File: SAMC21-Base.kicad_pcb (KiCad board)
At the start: 4 copper layers, 25.4 x 42.5 mm, 52 parts, among them J1 Conn_01x04, J2 Conn_01x10, J3 Conn_01x10, J5 Conn_ARM_JTAG_SWD_10, U1 ATSAMC21E18A-AUT, U2 TJA1043T, U3 TPS560430Y, U4 MCP1703A, Y1 8MHz

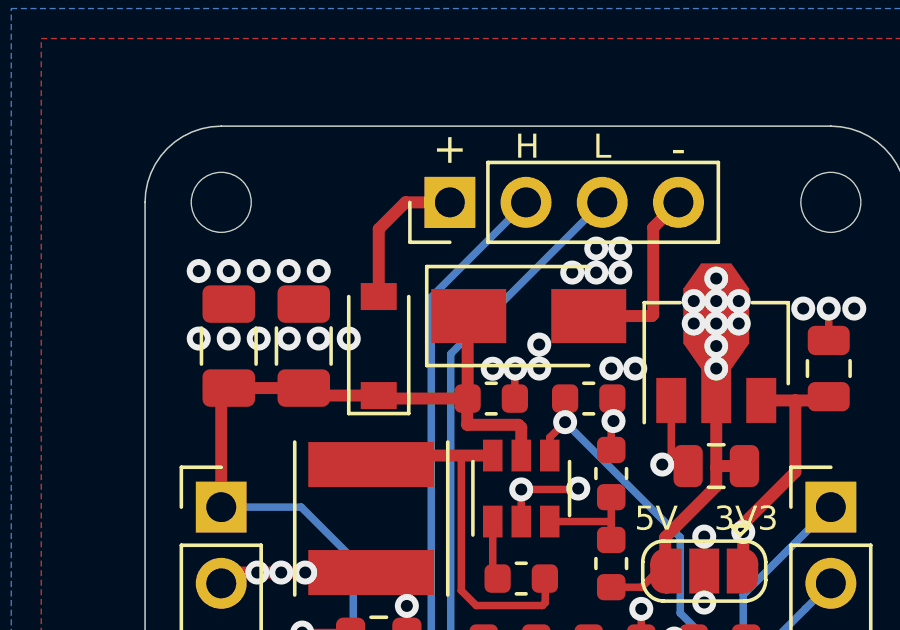
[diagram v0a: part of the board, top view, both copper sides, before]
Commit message: place ESD protection before polarity protection
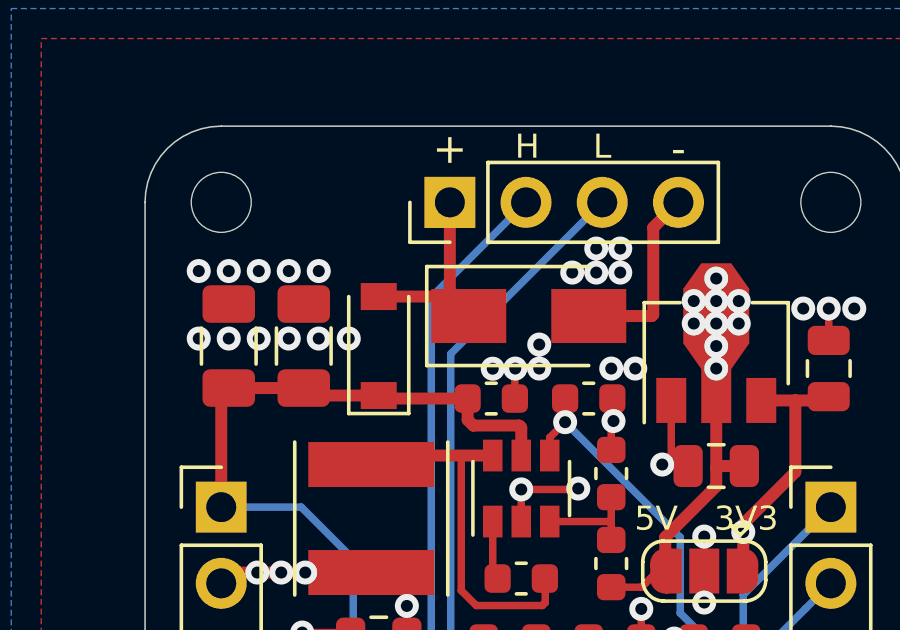
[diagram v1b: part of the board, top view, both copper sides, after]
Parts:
- L2: value L_Small -> MPZ1608S221A
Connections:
- D3 pad 1: +36V -> VBUS
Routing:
- net +36V: track 43.6 -> 40.7 mm
- net VBUS: track 4.99 -> 5.54 mm
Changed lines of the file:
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@@
     (thickness 1.6)
     (drawings 21)
-    (tracks 511)
+    (tracks 509)
     (zones 0)
     (modules 52)
@@
   )
   (setup
-    (last_trace_width 0.25)
+    (last_trace_width 0.4)
     (user_trace_width 0.25)
     (user_trace_width 0.4)
@@
       (net 43 GND))
     (pad 1 smd rect (at -2 0) (size 2.5 1.8) (layers F.Cu F.Paste F.Mask)
-      (net 2 +36V))
+      (net 12 VBUS))
     (model ${KISYS3DMOD}/Diode_SMD.3dshapes/D_SMA.wrl
       (at (xyz 0 0 0))
@@
       (effects (font (size 1 1) (thickness 0.15)))
     )
-    (fp_text value L_Small (at 0 1.43) (layer F.Fab)
+    (fp_text value MPZ1608S221A (at 0 1.43) (layer F.Fab)
       (effects (font (size 1 1) (thickness 0.15)))
     )
@@
   (segment (start 114.87 70.15) (end 114.8 70.08) (width 0.25) (layer F.Cu) (net 2))
   (segment (start 114.87 71.655) (end 114.87 70.15) (width 0.25) (layer F.Cu) (net 2))
-  (segment (start 111.6 60.85) (end 111.6 61.78) (width 0.4) (layer F.Cu) (net 2))
-  (segment (start 111.50501 60.75501) (end 111.6 60.85) (width 0.4) (layer F.Cu) (net 2))
-  (segment (start 109.8 60.75501) (end 111.50501 60.75501) (width 0.4) (layer F.Cu) (net 2))
-  (segment (start 109.8 59.8925) (end 109.8 60.75501) (width 0.4) (layer F.Cu) (net 2))
-  (segment (start 109.8125 59.88) (end 109.8 59.8925) (width 0.4) (layer F.Cu) (net 2))
   (segment (start 101.85 59.53) (end 104.35 59.53) (width 0.4) (layer F.Cu) (net 2))
   (segment (start 101.6 59.78) (end 101.85 59.53) (width 0.4) (layer F.Cu) (net 2))
@@
   (segment (start 106.95 59.88) (end 106.85 59.78) (width 0.4) (layer F.Cu) (net 2))
   (segment (start 109.8125 59.88) (end 106.95 59.88) (width 0.4) (layer F.Cu) (net 2))
-  (segment (start 109.8125 57.1675) (end 109.85 57.13) (width 0.4) (layer F.Cu) (net 2))
-  (segment (start 109.8125 59.88) (end 109.8125 57.1675) (width 0.4) (layer F.Cu) (net 2))
   (segment (start 107.8875 70.13) (end 107.8875 69.267508) (width 0.25) (layer F.Cu) (net 2))
   (segment (start 107.8875 69.267508) (end 107.85 69.230008) (width 0.25) (layer F.Cu) (net 2))
@@
   (segment (start 104.27 63.5) (end 106 65.23) (width 0.25) (layer B.Cu) (net 2))
   (segment (start 101.6 63.5) (end 104.27 63.5) (width 0.25) (layer B.Cu) (net 2))
+  (segment (start 111.6 60.85) (end 111.6 61.78) (width 0.4) (layer F.Cu) (net 2))
+  (segment (start 111.53 60.78) (end 111.6 60.85) (width 0.4) (layer F.Cu) (net 2))
+  (segment (start 110 60.78) (end 111.53 60.78) (width 0.4) (layer F.Cu) (net 2))
+  (segment (start 109.8125 60.5925) (end 110 60.78) (width 0.4) (layer F.Cu) (net 2))
+  (segment (start 109.8125 59.88) (end 109.8125 60.5925) (width 0.4) (layer F.Cu) (net 2))
   (via (at 118.1 58.88) (size 0.8) (drill 0.4) (layers F.Cu B.Cu) (net 3))
   (via (at 118.85 57.38) (size 0.8) (drill 0.4) (layers F.Cu B.Cu) (net 3))
@@
   (segment (start 119.1375 83.6175) (end 119.1375 85.63) (width 0.25) (layer F.Cu) (net 11))
   (segment (start 118.95 83.43) (end 119.1375 83.6175) (width 0.25) (layer F.Cu) (net 11))
-  (segment (start 107.74 53.34) (end 109.22 53.34) (width 0.4) (layer F.Cu) (net 12))
-  (segment (start 106.85 54.23) (end 107.74 53.34) (width 0.4) (layer F.Cu) (net 12))
-  (segment (start 106.85 56.48) (end 106.85 54.23) (width 0.4) (layer F.Cu) (net 12))
+  (segment (start 109.22 56.5) (end 109.22 53.34) (width 0.4) (layer F.Cu) (net 12))
+  (segment (start 109.2 56.48) (end 109.22 56.5) (width 0.4) (layer F.Cu) (net 12))
+  (segment (start 106.85 56.48) (end 109.2 56.48) (width 0.4) (layer F.Cu) (net 12))
   (segment (start 107.8875 90.38) (end 110.0625 90.38) (width 0.25) (layer F.Cu) (net 13))
   (segment (start 108.05 88.13) (end 107.497994 88.13) (width 0.25) (layer F.Cu) (net 14))

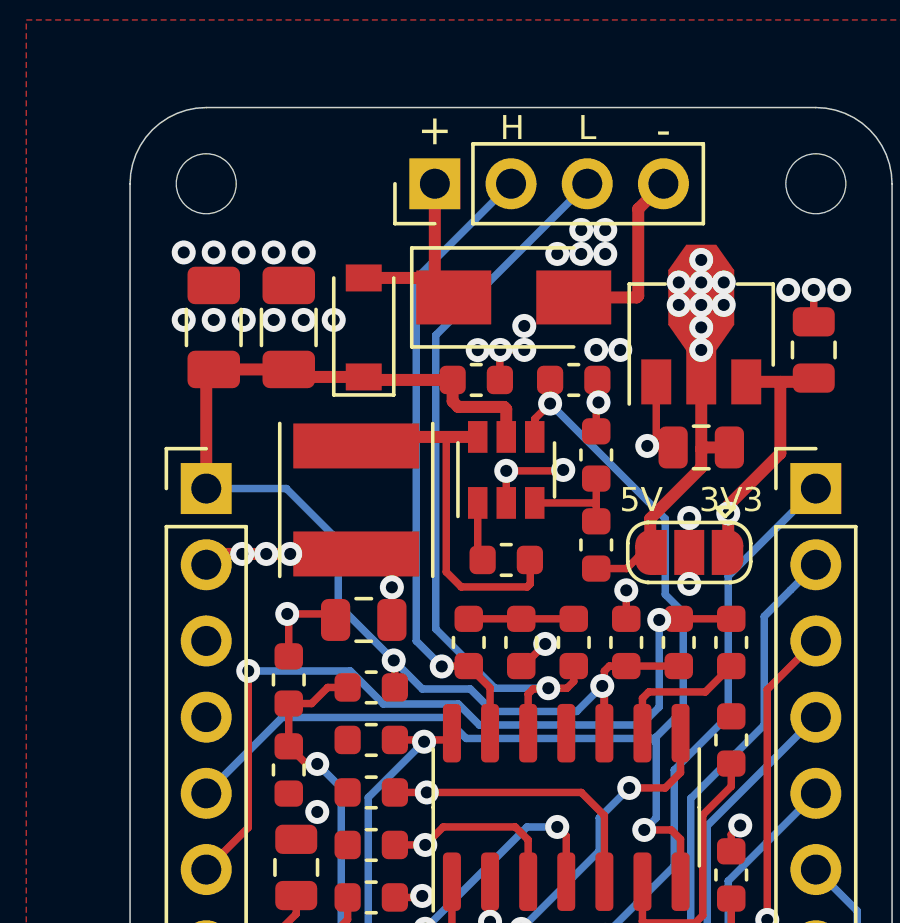
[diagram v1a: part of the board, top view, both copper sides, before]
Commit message: connect TJA1043 split pin
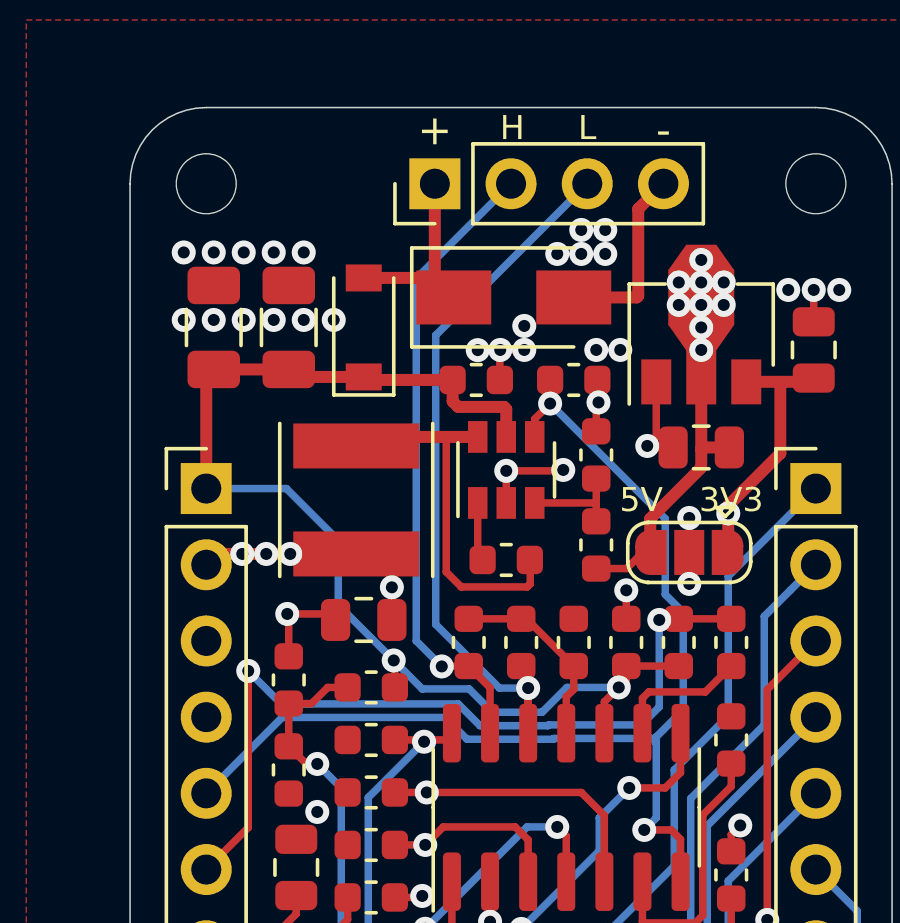
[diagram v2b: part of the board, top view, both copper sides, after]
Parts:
- C2: value 100nF/50V -> 100nF/100V
- R1: value 10K -> 100K
- moved C17 1.75 mm to (113.8, 68.6), turned to 270 degrees
- moved RT2 1.75 mm to (112.1, 68.6)
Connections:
- U2 pad 11: Net-(U2-Pad11) -> Net-(C17-Pad2)
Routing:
- net Net-(C17-Pad2): track 3.50 -> 6.49 mm
- net +36V: track 40.7 -> 39.4 mm
- net GND: track 37.9 -> 36.8 mm, vias 41 -> 40

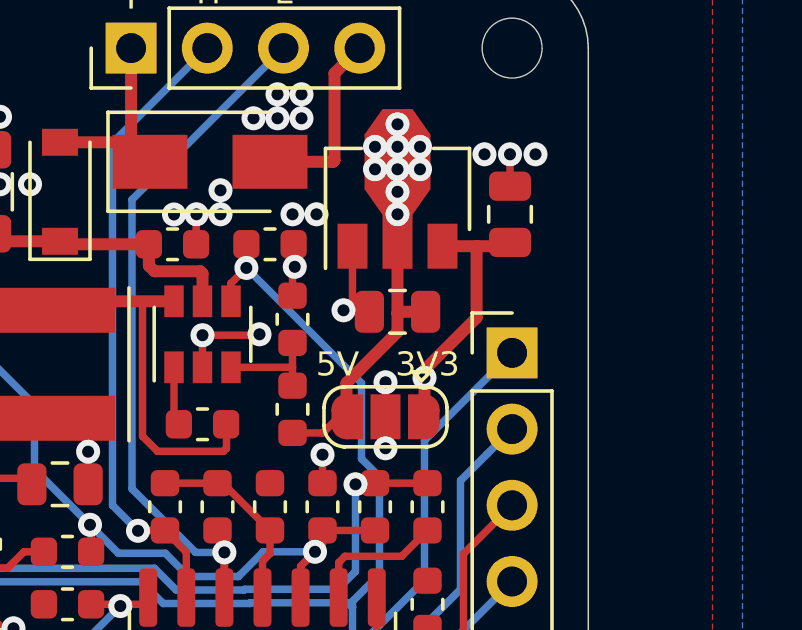
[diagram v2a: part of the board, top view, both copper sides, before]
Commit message: improve 3V3 routing
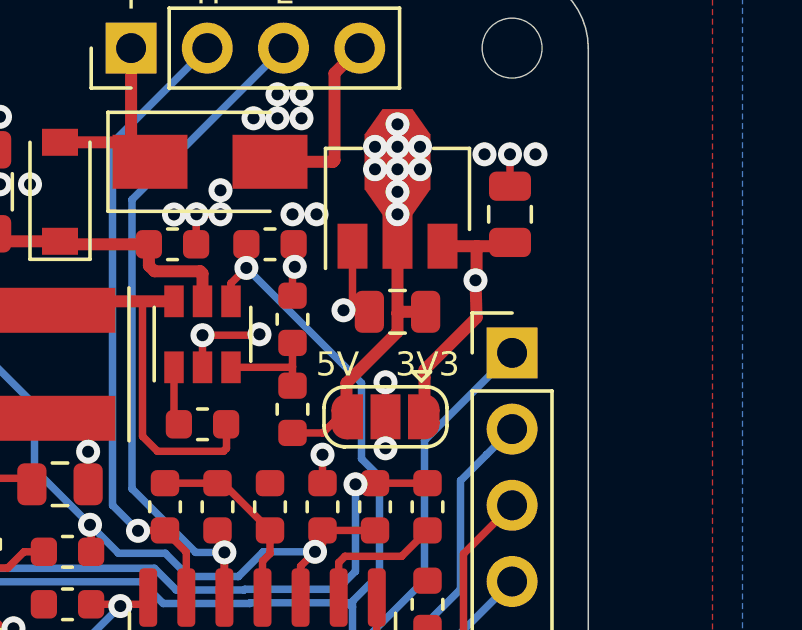
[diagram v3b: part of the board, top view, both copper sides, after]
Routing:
- net +3V3: track 28.0 -> 34.3 mm
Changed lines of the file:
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@@
     (thickness 1.6)
     (drawings 21)
-    (tracks 509)
+    (tracks 512)
     (zones 0)
     (modules 52)
@@
   )
   (setup
-    (last_trace_width 0.25)
+    (last_trace_width 0.4)
     (user_trace_width 0.25)
     (user_trace_width 0.4)
@@
   (segment (start 120.7365 59.9435) (end 121.724 59.9435) (width 0.4) (layer F.Cu) (net 4))
   (segment (start 119 65.63) (end 119 64.330006) (width 0.4) (layer F.Cu) (net 4))
-  (via (at 119 64.330006) (size 0.8) (drill 0.4) (layers F.Cu B.Cu) (net 4))
-  (segment (start 120.7365 59.9435) (end 120.7365 62.327821) (width 0.4) (layer F.Cu) (net 4))
   (segment (start 120.7365 62.327821) (end 119 64.064321) (width 0.4) (layer F.Cu) (net 4))
   (segment (start 119 64.064321) (end 119 64.330006) (width 0.4) (layer F.Cu) (net 4))
-  (segment (start 118.096001 65.533999) (end 119 64.63) (width 0.4) (layer In2.Cu) (net 4))
-  (segment (start 119 64.63) (end 119 64.330006) (width 0.4) (layer In2.Cu) (net 4))
-  (segment (start 105.850001 67.779999) (end 113.550001 67.779999) (width 0.4) (layer In2.Cu) (net 4))
-  (segment (start 105.05 68.58) (end 105.850001 67.779999) (width 0.4) (layer In2.Cu) (net 4))
-  (segment (start 115.796001 65.533999) (end 118.096001 65.533999) (width 0.4) (layer In2.Cu) (net 4))
-  (segment (start 113.550001 67.779999) (end 115.796001 65.533999) (width 0.4) (layer In2.Cu) (net 4))
+  (segment (start 120.7365 61.0435) (end 120.7 61.08) (width 0.4) (layer F.Cu) (net 4))
+  (segment (start 120.7365 59.9435) (end 120.7365 61.0435) (width 0.4) (layer F.Cu) (net 4))
+  (via (at 120.7 61.08) (size 0.8) (drill 0.4) (layers F.Cu B.Cu) (net 4))
+  (segment (start 120.7 61.08) (end 120.7365 62.327821) (width 0.4) (layer F.Cu) (net 4))
+  (segment (start 119.75 60.13) (end 120.7 61.08) (width 0.4) (layer In2.Cu) (net 4))
+  (segment (start 115.5 61.48) (end 116.85 60.13) (width 0.4) (layer In2.Cu) (net 4))
+  (segment (start 115.5 65.83) (end 115.5 61.48) (width 0.4) (layer In2.Cu) (net 4))
+  (segment (start 113.25 68.08) (end 115.5 65.83) (width 0.4) (layer In2.Cu) (net 4))
+  (segment (start 105.55 68.08) (end 113.25 68.08) (width 0.4) (layer In2.Cu) (net 4))
+  (segment (start 116.85 60.13) (end 119.75 60.13) (width 0.4) (layer In2.Cu) (net 4))
+  (segment (start 105.05 68.58) (end 105.55 68.08) (width 0.4) (layer In2.Cu) (net 4))
   (segment (start 101.6 68.58) (end 105.05 68.58) (width 0.4) (layer In2.Cu) (net 4))
   (segment (start 104.35 70.6675) (end 104.35 72.0925) (width 0.25) (layer F.Cu) (net 5))

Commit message: improve routing
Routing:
- net GND: track 36.8 -> 30.5 mm
- net CAN_L: track 24.6 -> 25.5 mm
- net +5V: track 44.2 -> 44.1 mm, vias 14 -> 13
- added copper zone on F.Cu, net +5V

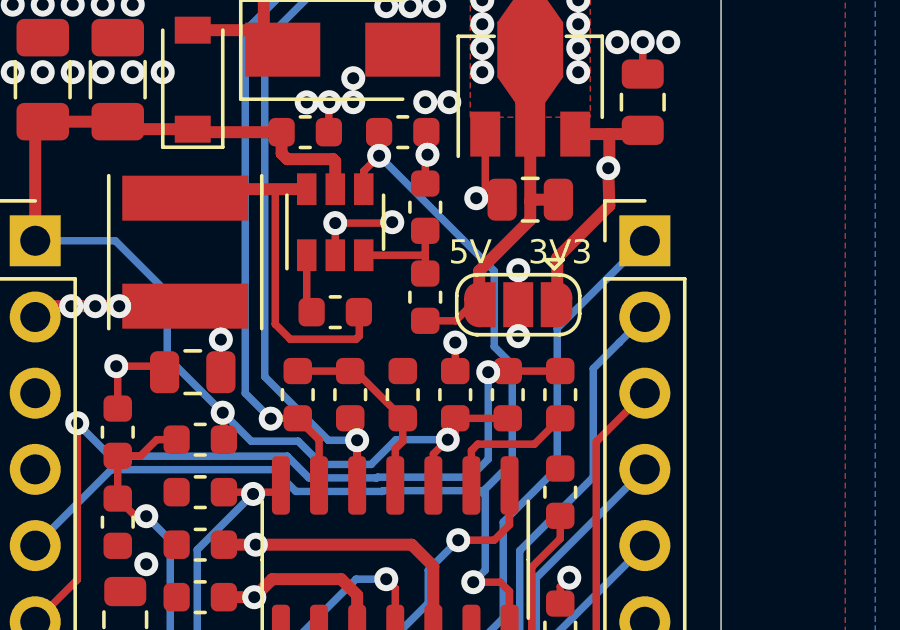
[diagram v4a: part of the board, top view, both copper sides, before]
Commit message: change VBUS_ACC volatge divider
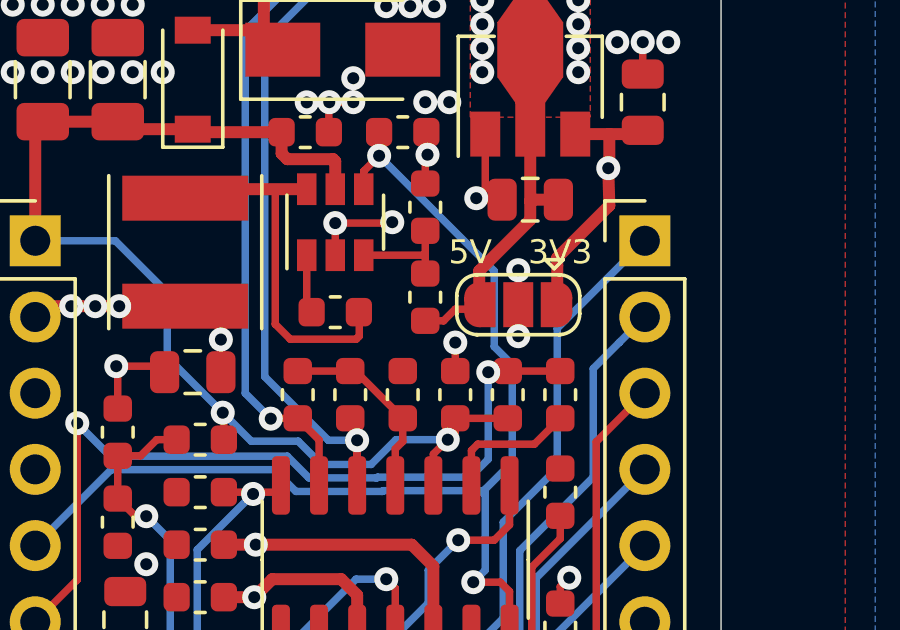
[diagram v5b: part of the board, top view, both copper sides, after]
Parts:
- C18, C19: value 9pF -> 18pF
- R10: value 4K7 -> 10K
- Y1: value 8MHz -> ABM3-8.000MHZ-D2Y-T
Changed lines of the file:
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@@
     (thickness 1.6)
     (drawings 21)
-    (tracks 513)
+    (tracks 514)
     (zones 0)
     (modules 52)
@@
       (effects (font (size 1 1) (thickness 0.15)))
     )
-    (fp_text value 8MHz (at 0 2.8 90) (layer F.Fab)
+    (fp_text value ABM3-8.000MHZ-D2Y-T (at 0 2.8 90) (layer F.Fab)
       (effects (font (size 1 1) (thickness 0.15)))
     )
@@
       (effects (font (size 1 1) (thickness 0.15)))
     )
-    (fp_text value 4K7 (at 0 1.43 90) (layer F.Fab)
+    (fp_text value 10K (at 0 1.43 90) (layer F.Fab)
       (effects (font (size 1 1) (thickness 0.15)))
     )
@@
       (effects (font (size 1 1) (thickness 0.15)))
     )
-    (fp_text value 9pF (at 0 1.43) (layer F.Fab)
+    (fp_text value 18pF (at 0 1.43) (layer F.Fab)
       (effects (font (size 1 1) (thickness 0.15)))
     )
@@
       (effects (font (size 1 1) (thickness 0.15)))
     )
-    (fp_text value 9pF (at 0 1.43 90) (layer F.Fab)
+    (fp_text value 18pF (at 0 1.43 90) (layer F.Fab)
       (effects (font (size 1 1) (thickness 0.15)))
     )
@@
   (segment (start 119.0375 62.13) (end 118.15 62.13) (width 0.4) (layer F.Cu) (net 3))
   (segment (start 118.1 59.797) (end 118.1 62.18) (width 0.4) (layer F.Cu) (net 3))
-  (segment (start 116.25 65.78) (end 116.4 65.63) (width 0.25) (layer F.Cu) (net 3))
-  (segment (start 116 65.78) (end 116.25 65.78) (width 0.25) (layer F.Cu) (net 3))
-  (segment (start 115.6125 66.1675) (end 116 65.78) (width 0.25) (layer F.Cu) (net 3))
-  (segment (start 114.6 66.1675) (end 115.6125 66.1675) (width 0.25) (layer F.Cu) (net 3))
   (segment (start 103.130001 74.910001) (end 103.9 75.68) (width 0.4) (layer In2.Cu) (net 3))
   (segment (start 100.999999 74.910001) (end 103.130001 74.910001) (width 0.4) (layer In2.Cu) (net 3))
@@
   (segment (start 109.5 74.78) (end 111.8 74.78) (width 0.4) (layer F.Cu) (net 3))
   (segment (start 108.9 75.38) (end 109.5 74.78) (width 0.4) (layer F.Cu) (net 3))
+  (segment (start 114.6 66.1675) (end 114.6 66.08) (width 0.25) (layer F.Cu) (net 3))
+  (segment (start 115.6 65.78) (end 116.25 65.78) (width 0.25) (layer F.Cu) (net 3))
+  (segment (start 116.25 65.78) (end 116.4 65.63) (width 0.25) (layer F.Cu) (net 3))
+  (segment (start 115.2125 66.1675) (end 115.6 65.78) (width 0.25) (layer F.Cu) (net 3))
+  (segment (start 114.6 66.1675) (end 115.2125 66.1675) (width 0.25) (layer F.Cu) (net 3))
   (segment (start 121.724 59.9435) (end 121.85 59.8175) (width 0.4) (layer F.Cu) (net 4))
   (segment (start 119.6 59.9435) (end 120.7365 59.9435) (width 0.4) (layer F.Cu) (net 4))
